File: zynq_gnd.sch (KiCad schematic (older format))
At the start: 1 part

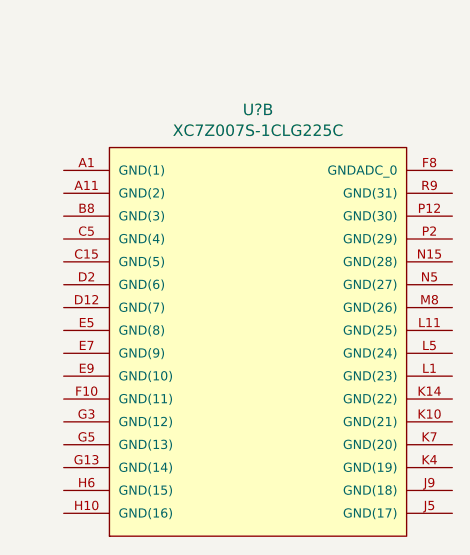
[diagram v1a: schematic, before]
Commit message: Update schematic sheets
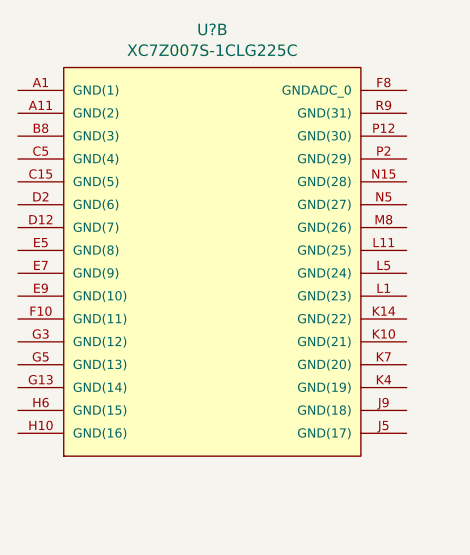
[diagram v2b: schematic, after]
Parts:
- removed U?: XC7Z007S-1CLG225C, BGA225C80P15X15_1300X1300X150, symbol XC7Z007S-1CLG225C:XC7Z007S-1CLG225C
- added U?: XC7Z007S-1CLG225C, BGA225C80P15X15_1300X1300X150, symbol XC7Z007S-1CLG225C:XC7Z007S-1CLG225C
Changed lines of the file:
@@
 $Descr A4 11693 8268
 encoding utf-8
-Sheet 5 7
+Sheet 7 7
 Title ""
 Date ""
@@
 $Comp
 L XC7Z007S-1CLG225C:XC7Z007S-1CLG225C U?
-U 2 1 675FFD36
-P 3050 3300
-F 0 "U?" H 3100 4365 50  0000 C CNN
-F 1 "XC7Z007S-1CLG225C" H 3100 4274 50  0000 C CNN
-F 2 "BGA225C80P15X15_1300X1300X150" H 3050 3300 50  0001 L BNN
-F 3 "" H 3050 3300 50  0001 L BNN
-F 4 "Xilinx Inc." H 3050 3300 50  0001 L BNN "MF"
-F 5 "FPGA Zynq-7000 Family 23000 Cells 667MHz 28nm 1V 225-Pin WCBGA Tray" H 3050 3300 50  0001 L BNN "DESCRIPTION"
-F 6 "CSPBGA-225 Xilinx" H 3050 3300 50  0001 L BNN "PACKAGE"
-F 7 "42.41 USD" H 3050 3300 50  0001 L BNN "PRICE"
-F 8 "CSPBGA-225 Xilinx" H 3050 3300 50  0001 L BNN "Package"
-F 9 "https://www.snapeda.com/parts/XC7Z007S-1CLG225C/Xilinx/view-part/?ref=eda" H 3050 3300 50  0001 L BNN "Check_prices"
-F 10 "None" H 3050 3300 50  0001 L BNN "Price"
-F 11 "https://www.snapeda.com/parts/XC7Z007S-1CLG225C/Xilinx/view-part/?ref=snap" H 3050 3300 50  0001 L BNN "SnapEDA_Link"
-F 12 "XC7Z007S-1CLG225C" H 3050 3300 50  0001 L BNN "MP"
-F 13 "\\n                        \\n                            Single ARM® Cortex®-A9 MPCore™ with CoreSight™ System On Chip (SOC) IC Zynq®-7000 Artix™-7 FPGA, 23K Logic Cells   667MHz 225-CSPBGA (13x13)\\n                        \\n" H 3050 3300 50  0001 L BNN "Description"
-F 14 "In Stock" H 3050 3300 50  0001 L BNN "Availability"
-F 15 "Bad" H 3050 3300 50  0001 L BNN "AVAILABILITY"
-F 16 "Xilinx" H 3050 3300 50  0001 L BNN "MANUFACTURER"
-	2    3050 3300
+U 2 1 675FA3E6
+P 2850 2950
+F 0 "U?" H 2900 4015 50  0000 C CNN
+F 1 "XC7Z007S-1CLG225C" H 2900 3924 50  0000 C CNN
+F 2 "BGA225C80P15X15_1300X1300X150" H 2850 2950 50  0001 L BNN
+F 3 "" H 2850 2950 50  0001 L BNN
+F 4 "Xilinx Inc." H 2850 2950 50  0001 L BNN "MF"
+F 5 "FPGA Zynq-7000 Family 23000 Cells 667MHz 28nm 1V 225-Pin WCBGA Tray" H 2850 2950 50  0001 L BNN "DESCRIPTION"
+F 6 "CSPBGA-225 Xilinx" H 2850 2950 50  0001 L BNN "PACKAGE"
+F 7 "42.41 USD" H 2850 2950 50  0001 L BNN "PRICE"
+F 8 "CSPBGA-225 Xilinx" H 2850 2950 50  0001 L BNN "Package"
+F 9 "https://www.snapeda.com/parts/XC7Z007S-1CLG225C/Xilinx/view-part/?ref=eda" H 2850 2950 50  0001 L BNN "Check_prices"
+F 10 "None" H 2850 2950 50  0001 L BNN "Price"
+F 11 "https://www.snapeda.com/parts/XC7Z007S-1CLG225C/Xilinx/view-part/?ref=snap" H 2850 2950 50  0001 L BNN "SnapEDA_Link"
+F 12 "XC7Z007S-1CLG225C" H 2850 2950 50  0001 L BNN "MP"
+F 13 "\\n                        \\n                            Single ARM® Cortex®-A9 MPCore™ with CoreSight™ System On Chip (SOC) IC Zynq®-7000 Artix™-7 FPGA, 23K Logic Cells   667MHz 225-CSPBGA (13x13)\\n                        \\n" H 2850 2950 50  0001 L BNN "Description"
+F 14 "In Stock" H 2850 2950 50  0001 L BNN "Availability"
+F 15 "Bad" H 2850 2950 50  0001 L BNN "AVAILABILITY"
+F 16 "Xilinx" H 2850 2950 50  0001 L BNN "MANUFACTURER"
+	2    2850 2950
 	1    0    0    -1
 $EndComp
